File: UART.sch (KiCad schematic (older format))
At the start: 12 parts, among them P3 CONN_01X04, P5 CONN_01X04, P6 CONN_01X04, U4 MAX3227

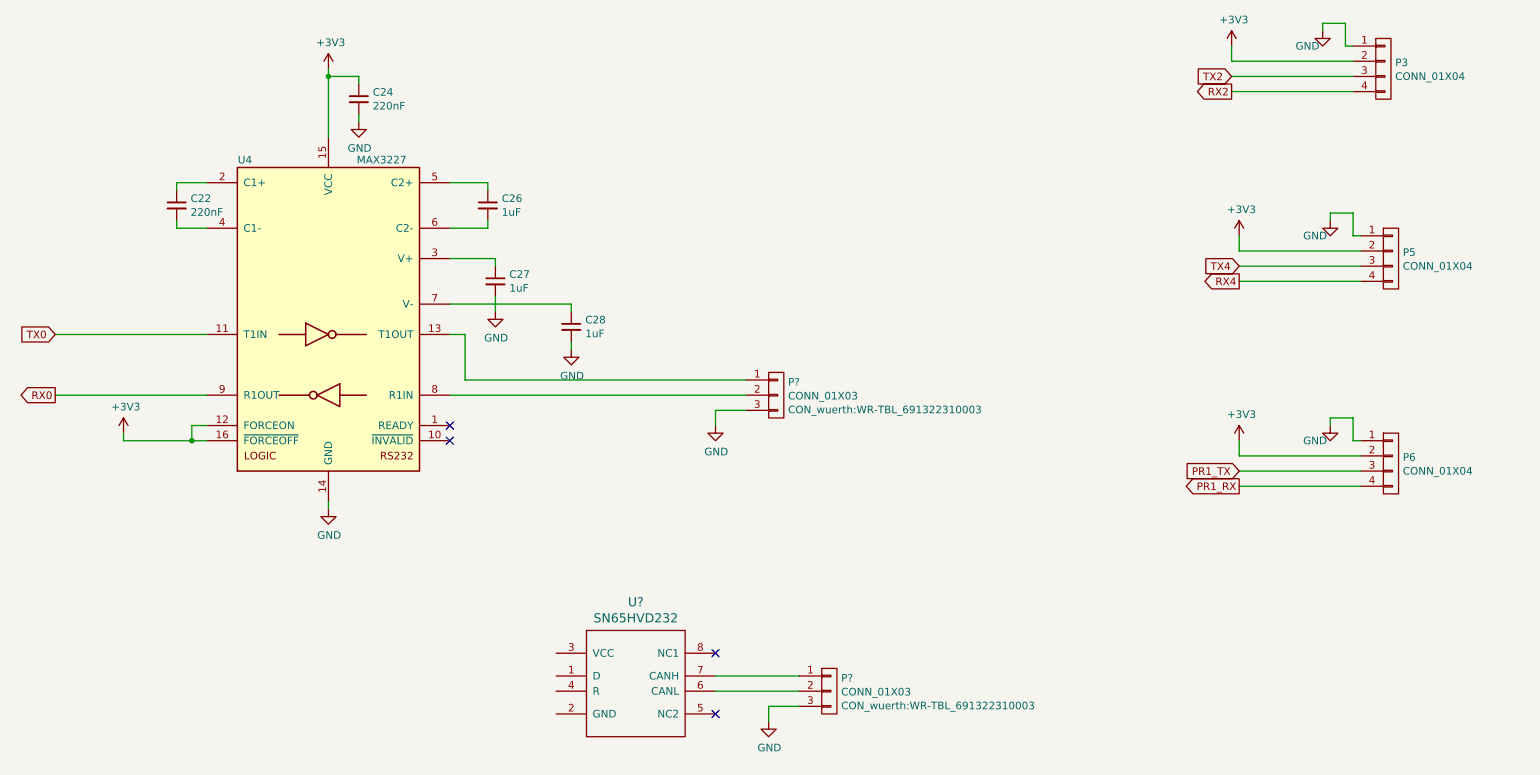
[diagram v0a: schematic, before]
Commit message: added can bus
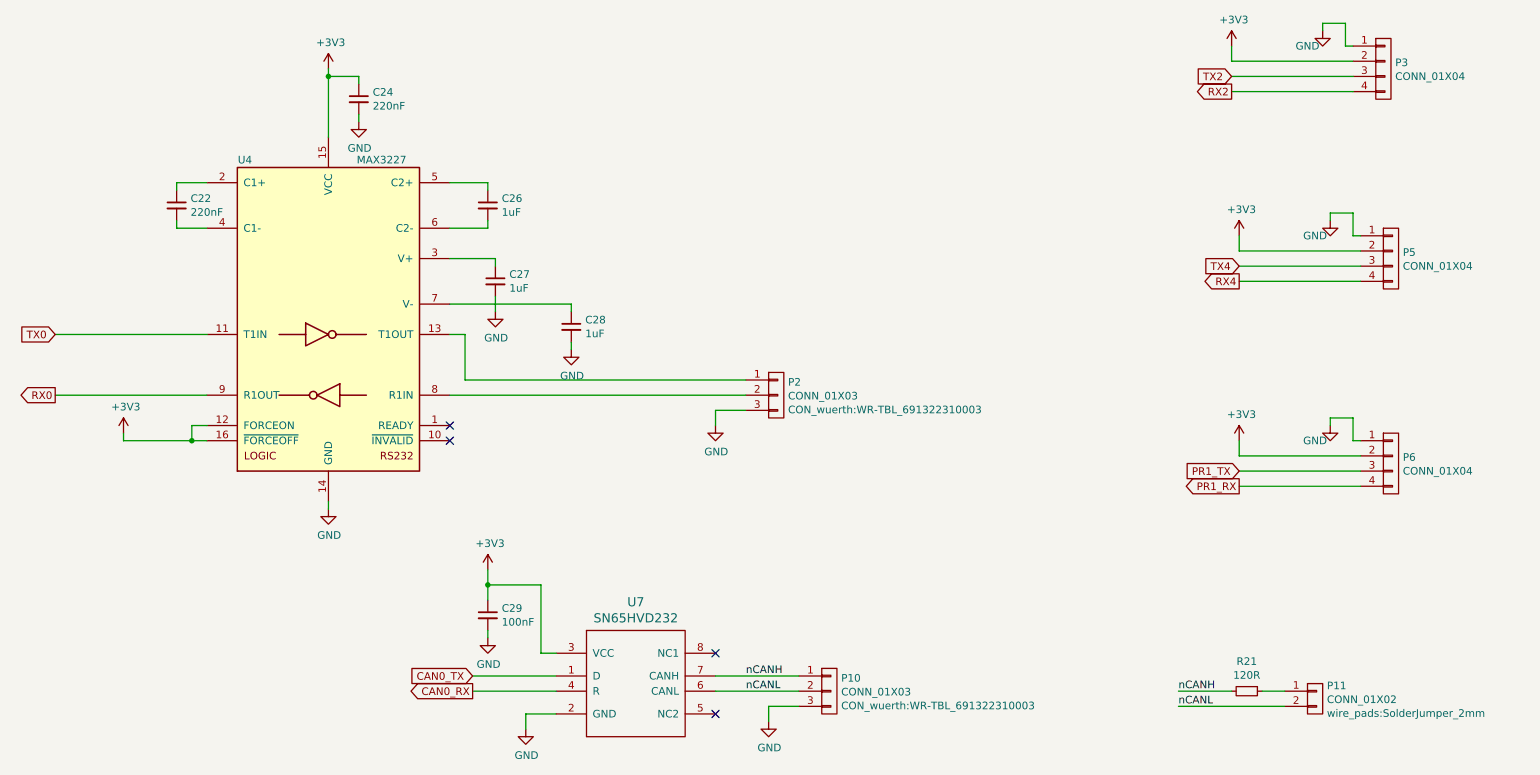
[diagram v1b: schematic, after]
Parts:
- added C29: 100nF, capacitors:C_0603, symbol devices:C_0603
- added P11: CONN_01X02, wire_pads:SolderJumper_2mm, symbol mechanical-connectors:CONN_01X02
- added R21: 120R, resistors:R_0603, symbol devices:R_0603
- gave numbers to parts that had none: 3
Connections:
- net +3V3: now also U7.3 (VCC), C29.1
- net GND: now also U7.2 (GND), C29.2
- net nCANH: now reaches P10.1 (P1), U7.7 (CANH)
- net nCANH: now also R21.2
- net nCANL: now reaches P10.2 (P2), U7.6 (CANL)
- net nCANL: now also P11.2 (P2)
- net CAN0_TX: now reaches U7.1 (D)
- net CAN0_RX: now reaches U7.4 (R)
- new net: P11.1 (P1), R21.1
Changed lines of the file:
@@
 	5750 3550 5750 3650
 $Comp
-L mechanical-connectors:CONN_01X03 P?
+L mechanical-connectors:CONN_01X03 P2
 U 1 1 5FE08D5C
 P 6150 3450
-F 0 "P?" H 6228 3536 50  0000 L CNN
+F 0 "P2" H 6228 3536 50  0000 L CNN
 F 1 "CONN_01X03" H 6228 3445 50  0000 L CNN
 F 2 "CON_wuerth:WR-TBL_691322310003" H 6228 3354 50  0000 L CNN
@@
 $EndComp
 $Comp
-L mechanical-connectors:CONN_01X03 P?
+L mechanical-connectors:CONN_01X03 P10
 U 1 1 5FE14388
 P 6500 5400
-F 0 "P?" H 6578 5486 50  0000 L CNN
+F 0 "P10" H 6578 5486 50  0000 L CNN
 F 1 "CONN_01X03" H 6578 5395 50  0000 L CNN
 F 2 "CON_wuerth:WR-TBL_691322310003" H 6578 5304 50  0000 L CNN
@@
 $EndComp
 $Comp
-L CAN-transceiver:SN65HVD232 U?
+L CAN-transceiver:SN65HVD232 U7
 U 1 1 5FE154CA
 P 4700 5700
-F 0 "U?" H 5225 6587 60  0000 C CNN
+F 0 "U7" H 5225 6587 60  0000 C CNN
 F 1 "SN65HVD232" H 5225 6481 60  0000 C CNN
 F 2 "SOIC:SOIJ-8_5.3x5.3mm_Pitch1.27mm" H 5550 5650 60  0001 C CNN
@@
 	6300 5500 6100 5500
 $Comp
-L power-supply:GND #PWR?
+L power-supply:GND #PWR0151
 U 1 1 5FE1EAD5
 P 6100 5600
-AR Path="/5FCC65EC/5FE1EAD5" Ref="#PWR?"  Part="1"
+AR Path="/5FCC65EC/5FE1EAD5" Ref="#PWR0151"  Part="1"
 AR Path="/600B38DA/5FE1EAD5" Ref="#PWR?"  Part="1"
-F 0 "#PWR?" H 6100 5350 50  0001 C CNN
+F 0 "#PWR0151" H 6100 5350 50  0001 C CNN
 F 1 "GND" H 6105 5427 50  0000 C CNN
 F 2 "" H 6100 5600 50  0000 C CNN
@@
 NoConn ~ 5750 5150
 NoConn ~ 5750 5550
+$Comp
+L devices:C_0603 C29
+U 1 1 5FD8282E
+P 4250 4900
+F 0 "C29" H 4342 4946 50  0000 L CNN
+F 1 "100nF" H 4342 4855 50  0000 L CNN
+F 2 "capacitors:C_0603" H 4250 4750 50  0001 C CNN
+F 3 "" H 4250 4900 50  0000 C CNN
+	1    4250 4900
+	1    0    0    -1
+$EndComp
+Wire Wire Line
+	4700 5150 4600 5150
+Wire Wire Line
+	4600 5150 4600 4700
+Wire Wire Line
+	4600 4700 4250 4700
+Wire Wire Line
+	4250 4700 4250 4800
+Wire Wire Line
+	4250 4700 4250 4600
+Connection ~ 4250 4700
+Wire Wire Line
+	4250 5000 4250 5050
+$Comp
+L power-supply:GND #PWR0148
+U 1 1 5FD87A70
+P 4250 5050
+AR Path="/5FCC65EC/5FD87A70" Ref="#PWR0148"  Part="1"
+AR Path="/600B38DA/5FD87A70" Ref="#PWR?"  Part="1"
+F 0 "#PWR0148" H 4250 4800 50  0001 C CNN
+F 1 "GND" H 4255 4877 50  0000 C CNN
+F 2 "" H 4250 5050 50  0000 C CNN
+F 3 "" H 4250 5050 50  0000 C CNN
+	1    4250 5050
+	1    0    0    -1
+$EndComp
+$Comp
+L power-supply:+3V3 #PWR0152
+U 1 1 5FD89495
+P 4250 4600
+AR Path="/5FCC65EC/5FD89495" Ref="#PWR0152"  Part="1"
+AR Path="/600B38DA/5FD89495" Ref="#PWR?"  Part="1"
+F 0 "#PWR0152" H 4250 4450 50  0001 C CNN
+F 1 "+3V3" H 4265 4773 50  0000 C CNN
+F 2 "" H 4250 4600 50  0000 C CNN
+F 3 "" H 4250 4600 50  0000 C CNN
+	1    4250 4600
+	1    0    0    -1
+$EndComp
+Wire Wire Line
+	4700 5550 4500 5550
+$Comp
+L power-supply:GND #PWR0155
+U 1 1 5FD8A810
+P 4500 5650
+AR Path="/5FCC65EC/5FD8A810" Ref="#PWR0155"  Part="1"
+AR Path="/600B38DA/5FD8A810" Ref="#PWR?"  Part="1"
+F 0 "#PWR0155" H 4500 5400 50  0001 C CNN
+F 1 "GND" H 4505 5477 50  0000 C CNN
+F 2 "" H 4500 5650 50  0000 C CNN
+F 3 "" H 4500 5650 50  0000 C CNN
+	1    4500 5650
+	1    0    0    -1
+$EndComp
+Wire Wire Line
+	4500 5550 4500 5650
+Wire Wire Line
+	4700 5400 4150 5400
+Wire Wire Line
+	4700 5300 4150 5300
+Text GLabel 4150 5400 0    50   Output ~ 0
+CAN0_RX
+Text GLabel 4150 5300 0    50   Input ~ 0
+CAN0_TX
+Text Label 5950 5300 0    50   ~ 0
+nCANH
+Text Label 5950 5400 0    50   ~ 0
+nCANL
+$Comp
+L devices:R_0603 R21
+U 1 1 5FD986DB
+P 9250 5400
+F 0 "R21" V 9054 5400 50  0000 C CNN
+F 1 "120R" V 9145 5400 50  0000 C CNN
+F 2 "resistors:R_0603" H 9250 5250 50  0001 C CNN
+F 3 "" H 9250 5400 50  0000 C CNN
+	1    9250 5400
+	0    1    1    0
+$EndComp
+Wire Wire Line
+	9150 5400 8800 5400
+Wire Wire Line
+	9350 5400 9500 5400
+$Comp
+L mechanical-connectors:CONN_01X02 P11
+U 1 1 5FD9D470
+P 9700 5450
+F 0 "P11" H 9778 5536 50  0000 L CNN
+F 1 "CONN_01X02" H 9778 5445 50  0000 L CNN
+F 2 "wire_pads:SolderJumper_2mm" H 9778 5354 50  0000 L CNN
+F 3 "" H 9700 5450 50  0000 C CNN
+	1    9700 5450
+	1    0    0    -1
+$EndComp
+Wire Wire Line
+	9500 5500 8800 5500
+Text Label 8800 5400 0    50   ~ 0
+nCANH
+Text Label 8800 5500 0    50   ~ 0
+nCANL
 $EndSCHEMATC
